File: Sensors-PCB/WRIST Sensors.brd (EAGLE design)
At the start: 53.5 x 9.1 mm, 22 parts, among them U1 VL6180X, U10 VL6180X, U2 VL6180X, U3 VL6180X, U4 VL6180X, U5 VL6180X, U6 VL6180X, U7 VL6180X, U8 VL6180X, U9 VL6180X

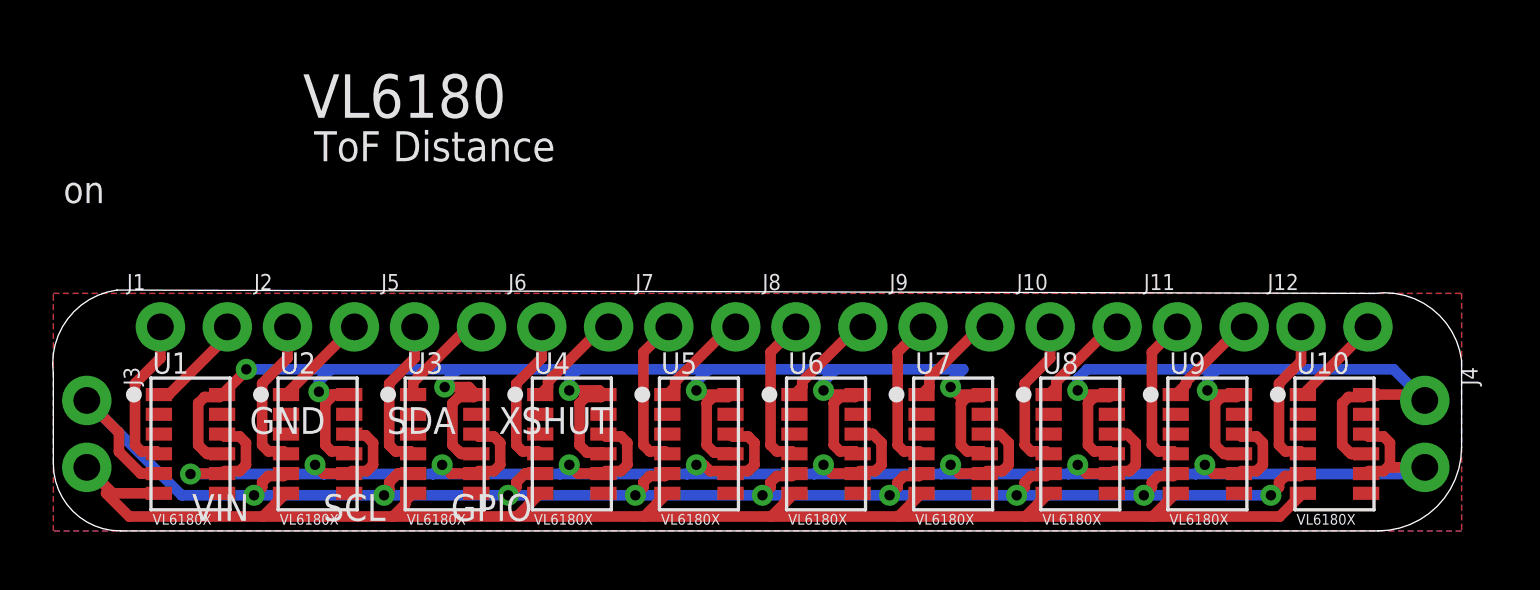
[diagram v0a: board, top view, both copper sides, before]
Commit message: add 20 pin header and rename board
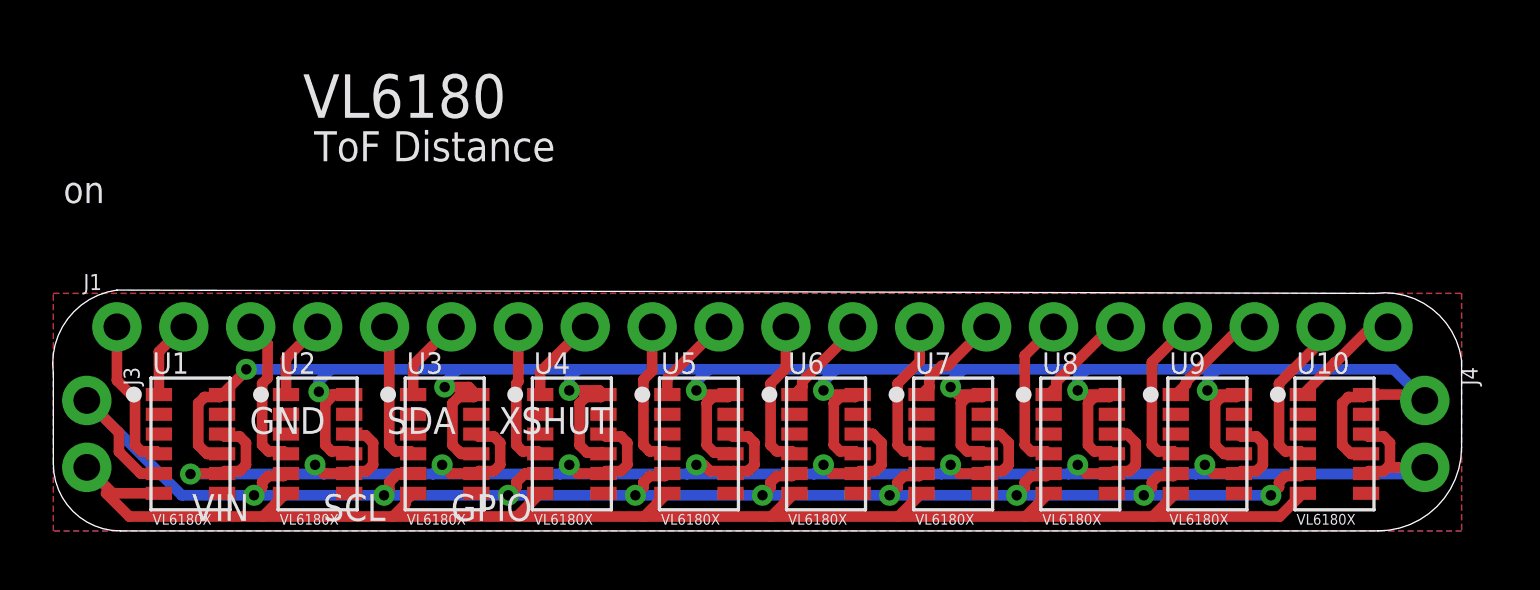
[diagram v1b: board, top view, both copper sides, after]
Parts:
- removed J10, J11, J12, J2, J5, J6, J7, J8, J9: (no value), SparkFun-Connectors:1X02_NO_SILK
- J1: device SparkFun-Connectors:1X02_NO_SILK -> SparkFun-Connectors:1X20_NOSILK
- moved J1 1.65 mm to (2.41, 7.75)
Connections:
- net GPIO_10: now also J1.20; no longer J12.2
- net GPIO_2: now also J1.4; no longer J2.2
- net GPIO_3: now also J1.6; no longer J5.2
- net GPIO_4: now also J1.8; no longer J6.2
- net GPIO_5: now also J1.10; no longer J7.2
- net GPIO_6: now also J1.12; no longer J8.2
- net GPIO_7: now also J1.14; no longer J9.2
- net GPIO_8: now also J1.16; no longer J10.2
- net GPIO_9: now also J1.18; no longer J11.2
- net XSHUT_10_2.8V: now also J1.19; no longer J12.1
- net XSHUT_2_2.8V: now also J1.3; no longer J2.1
- net XSHUT_3_2.8V: now also J1.5; no longer J5.1
- net XSHUT_4_2.8V: now also J1.7; no longer J6.1
- net XSHUT_5_2.8V: now also J1.9; no longer J7.1
- net XSHUT_6_2.8V: now also J1.11; no longer J8.1
- net XSHUT_7_2.8V: now also J1.13; no longer J9.1
- net XSHUT_8_2.8V: now also J1.15; no longer J10.1
- net XSHUT_9_2.8V: now also J1.17; no longer J11.1
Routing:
- net GND: track 99.2 -> 103.9 mm
- net GPIO_1: track 3.87 -> 2.96 mm
- net GPIO_3: track 3.93 -> 3.17 mm
- net GPIO_10: track 3.59 -> 4.30 mm
- net GPIO_2: track 3.66 -> 3.07 mm

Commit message: add gerber files
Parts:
- moved U1 0.25 mm to (5.21, 3.56)
- moved U10 0.25 mm to (48.6, 3.56)
- moved U2 0.25 mm to (10.0, 3.56)
- moved U3 0.25 mm to (14.9, 3.56)
- moved U4 0.25 mm to (19.7, 3.56)
- moved U5 0.25 mm to (24.5, 3.56)
- moved U6 0.25 mm to (29.3, 3.56)
- moved U7 0.25 mm to (34.2, 3.56)
- moved U8 0.25 mm to (39.0, 3.56)
- moved U9 0.25 mm to (43.8, 3.56)
- moved J1 0.25 mm to (2.41, 8.00)
- moved J3 0.25 mm to (1.27, 5.21)
- moved J4 0.25 mm to (52.1, 5.21)
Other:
- board size 53.5 x 9.1 mm -> 53.5 x 10.2 mm
- board text removed: "GND"
- board text removed: "GPIO"
- board text removed: "SCL"
- board text removed: "SDA"
- board text removed: "ToF Distance"
- board text removed: "VIN"
- board text removed: "VL6180"
- board text removed: "XSHUT"
- board text removed: "on"
